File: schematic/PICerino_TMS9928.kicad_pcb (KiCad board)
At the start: 2 copper layers, 101.7 x 107.1 mm, 61 parts, among them CON1 PICERINO-EDGE, J1 Conn_01x02, J10 Conn_01x08, J11 Conn_01x08, J12 Conn_01x03, J2 Y_Conn_01x02, J3 BY_Conn_01x02, J4 RY_Conn_01x02, J7 Conn_01x02, J8 Conn_01x02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

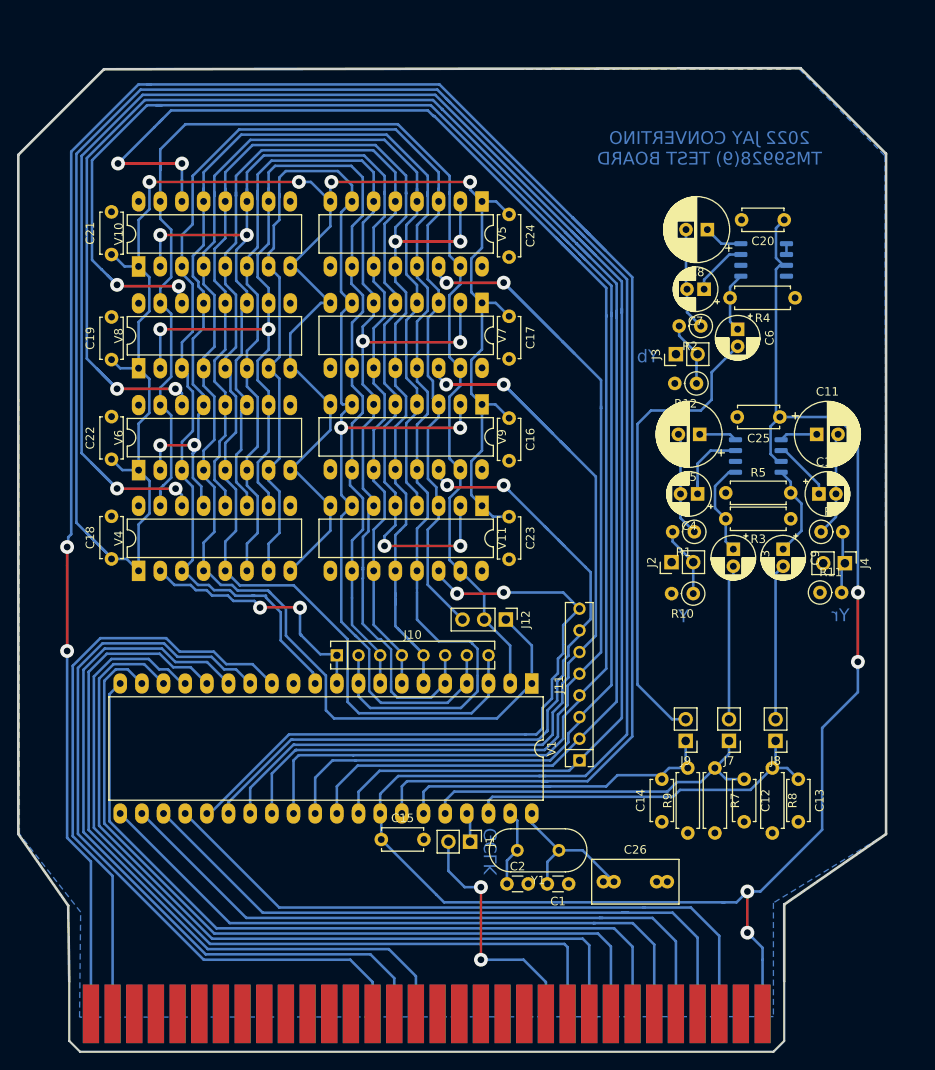
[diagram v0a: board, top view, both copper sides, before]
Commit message: updated schematic of TMS9928. This will work for 9918, and 9929 as well. Only Y is needed for 9918, and 9929 requires a different crystal. One item to point out is this video circuit is only supposed to be a buffer AC output. This isn't correct for Y on the component video. It does work with the retrotink-2x and gefen component to hdmi converters. haven't tested for a strong blue issue yet, doesn't seem to do that. Also jumpers are inserted on the board to bring out TMS99XX video signals out to whatever video circuit is desired
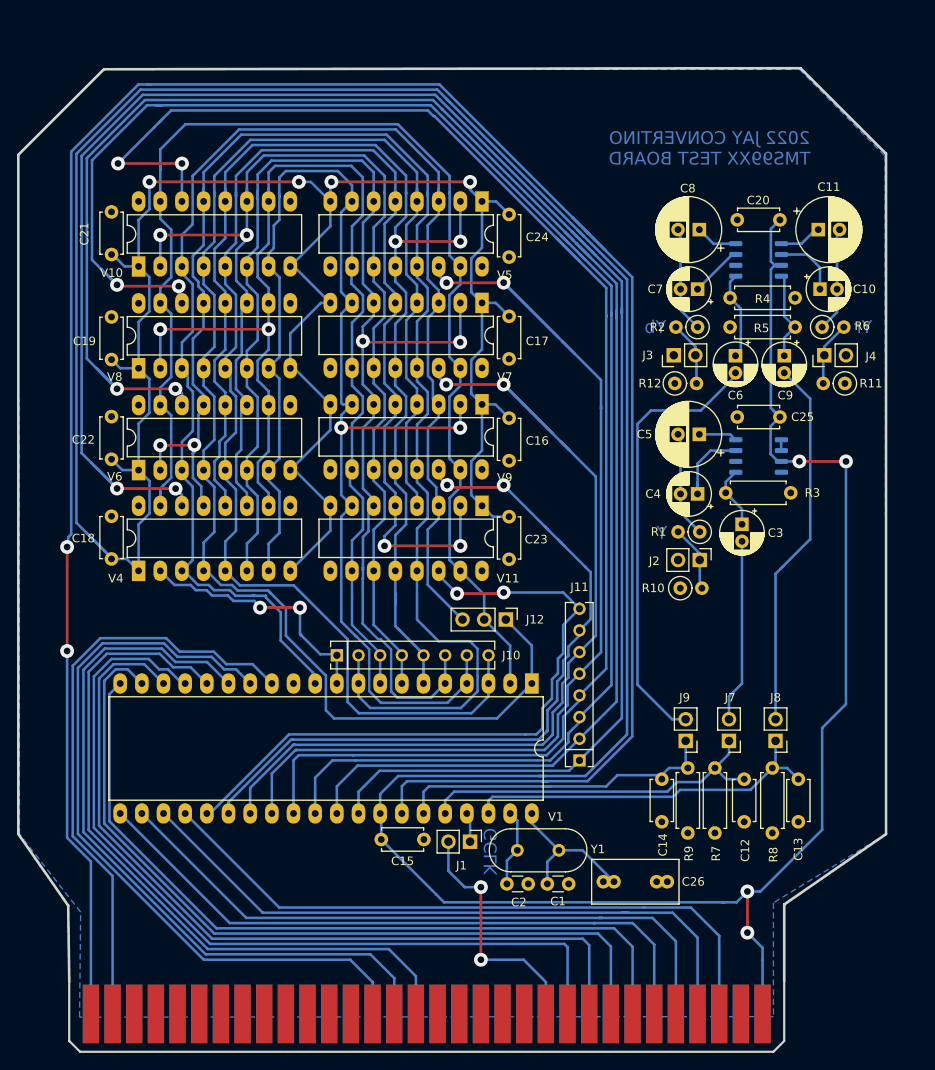
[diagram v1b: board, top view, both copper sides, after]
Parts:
- moved R11 24.7 mm to (202.9, 75.9), turned to 180 degrees
- moved J4 24.5 mm to (200.5, 72.6), turned to 90 degrees
- moved C11 24.0 mm to (199.8, 57.9)
- moved C10 24.0 mm to (200.0, 64.9)
- moved R6 24.0 mm to (200.3, 69.3)
- moved C9 22.7 mm to (195.8, 72.7)
- moved R5 19.4 mm to (189.5, 69.3)
- moved R4 7.62 mm to (189.5, 65.9), turned to 0 degrees
- moved J2 3.31 mm to (185.9, 96.6), turned to 270 degrees
- moved C6 3.12 mm to (190.1, 72.7)
- moved C3 3.09 mm to (190.9, 92.5)
- moved R3 3.05 mm to (196.6, 88.8)
- moved R12 2.54 mm to (183.0, 75.9), turned to 0 degrees
- moved R10 1.65 mm to (183.6, 99.9), turned to 0 degrees
- moved C8 0.94 mm to (185.9, 57.9)
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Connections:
- J2 pad 1: VSS -> Net-(J2-Pad1)
- J2 pad 2: Net-(J2-Pad2) -> VSS
- R1 pad 2: Net-(J2-Pad2) -> Net-(J2-Pad1)
- R10 pad 1: Net-(J2-Pad2) -> VSS
- R10 pad 2: Net-(R10-Pad2) -> Net-(J2-Pad1)
- R12 pad 1: Net-(J3-Pad2) -> VSS
- R12 pad 2: VSS -> Net-(J3-Pad2)
- R4 pad 1: VSS -> Net-(C6-Pad1)
- R4 pad 2: Net-(C6-Pad1) -> VSS
- V2 pad 5: Net-(C11-Pad1) -> Net-(V2-Pad5)
- V2 pad 6: Net-(C10-Pad1) -> Net-(V2-Pad5)
- V2 pad 8: Net-(C9-Pad1) -> VSS
- V3 pad 5: Net-(V3-Pad5) -> Net-(C11-Pad1)
- V3 pad 6: Net-(V3-Pad5) -> Net-(C10-Pad1)
- V3 pad 8: VSS -> Net-(C9-Pad1)
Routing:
- net Net-(C9-Pad2): track 18.3 -> 43.9 mm
- net Net-(J2-Pad2): track 8.60 -> 0.00 mm
- net Net-(J2-Pad1): track 0.00 -> 7.76 mm
- net VCC: track 608.0 -> 604.1 mm
- net Net-(C3-Pad2): track 18.1 -> 21.5 mm
- net Net-(C6-Pad1): track 7.11 -> 10.4 mm
- net Net-(C6-Pad2): track 55.3 -> 52.1 mm
- net Net-(C3-Pad1): track 11.4 -> 8.26 mm
- net Net-(V3-Pad5): track 1.27 -> 0.00 mm
- net Net-(V2-Pad5): track 0.00 -> 1.27 mm
- net Net-(C7-Pad2): track 12.0 -> 12.8 mm
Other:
- board text added: "2022 JAY CONVERTINO TMS99XX TEST BOARD"
- board text removed: "2022 JAY CONVERTINO TMS9928(9) TEST BOARD"

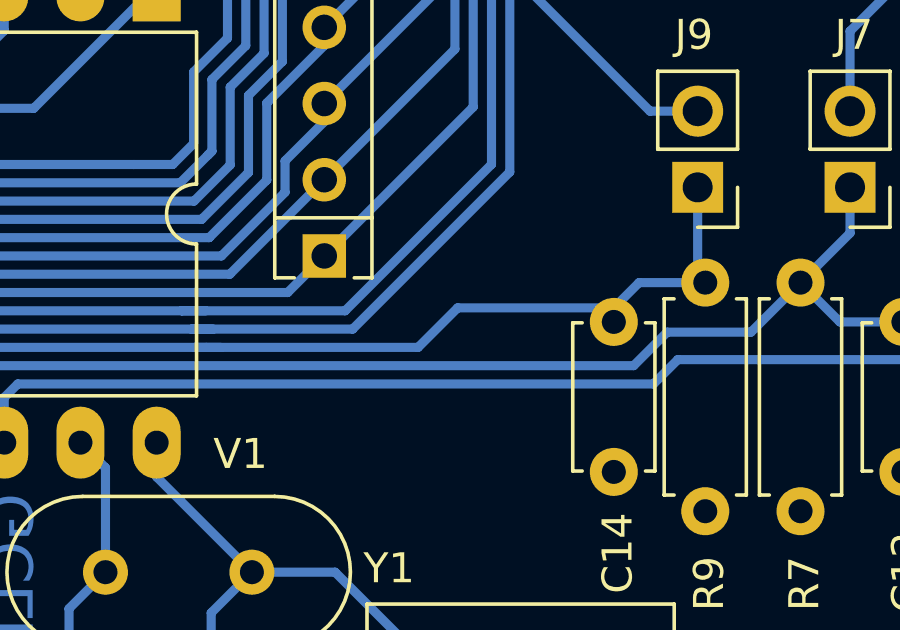
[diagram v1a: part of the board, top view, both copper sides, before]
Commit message: schematic cleanup in progress. changed address/write data lines to bus. cleaned up some component stuffs.
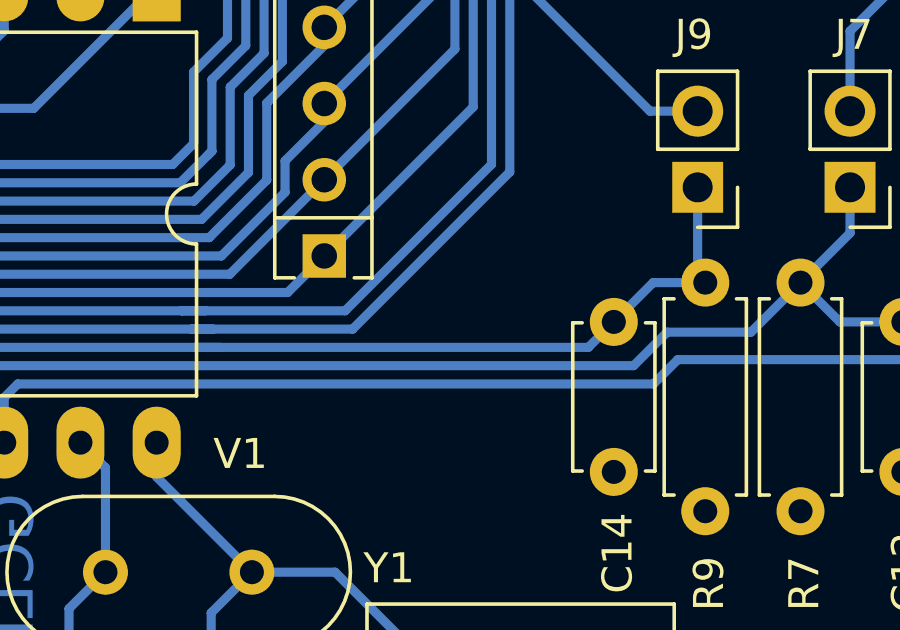
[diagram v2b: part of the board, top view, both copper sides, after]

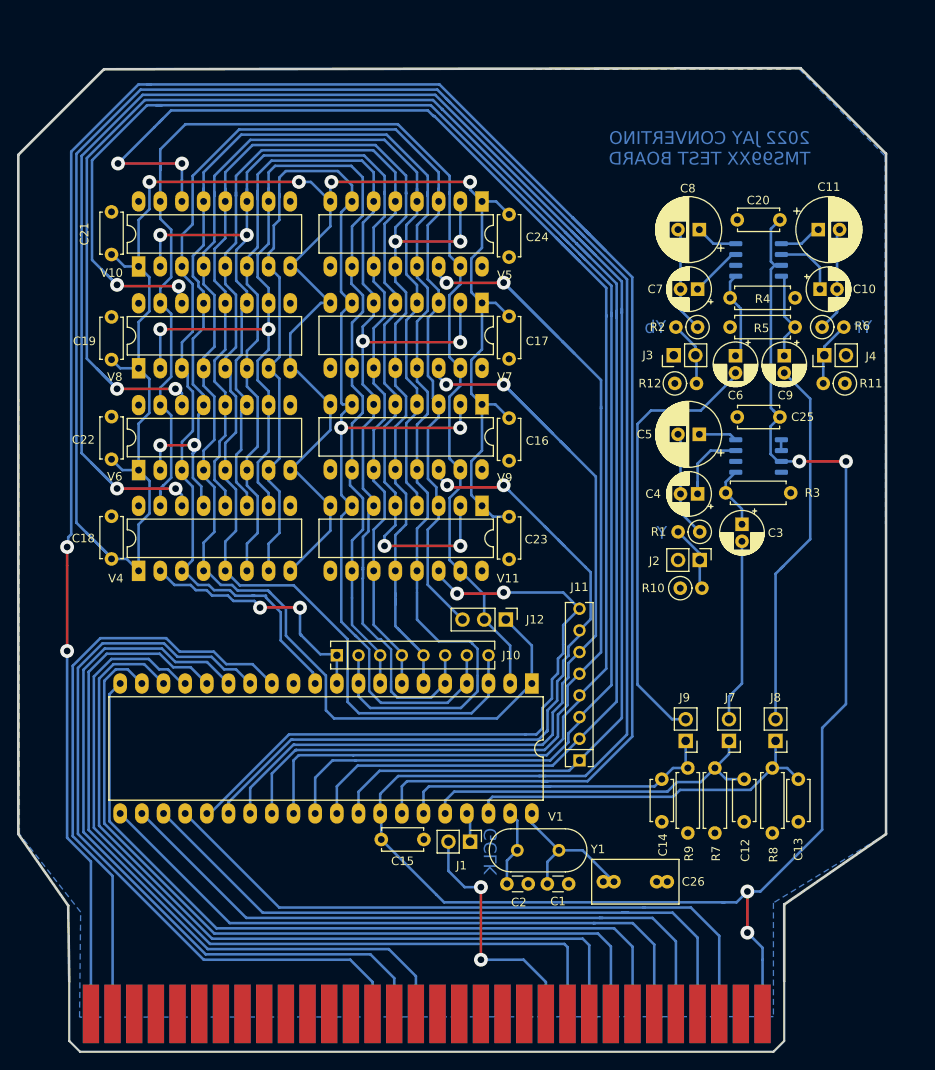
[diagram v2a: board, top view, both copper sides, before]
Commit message: major change to video section. dark green seemed off. tested adg453 sending output to gnd on that negative sync pulse. worked well. using mostly ti's idea with a modern sync strip ic. decided to use the other left over video opamp for a dc output. not tested at all but will be interesting since Y is supposed to be dc offset (works as ac offset though...whatever). This is intended to be a adjustable and usable for both the 9918 and 9928.
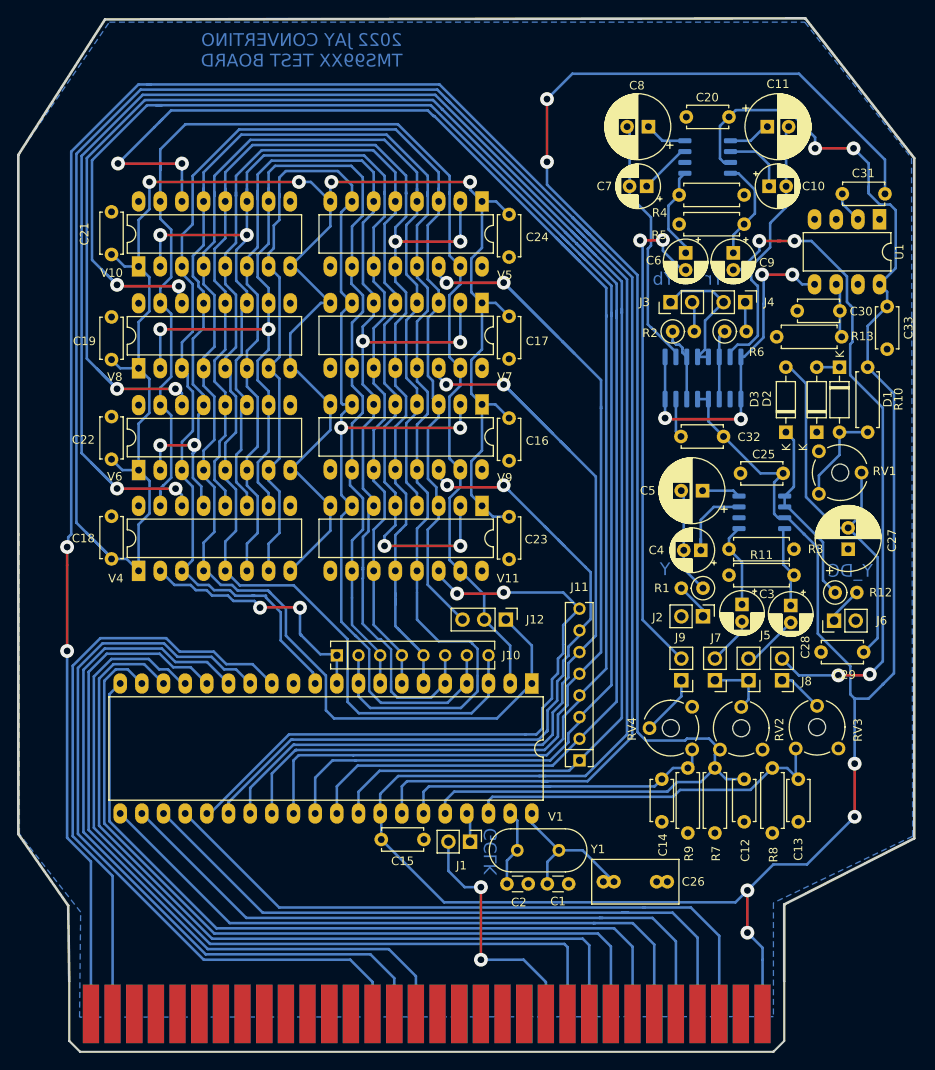
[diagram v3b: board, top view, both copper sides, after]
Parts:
- added C27: 100uF, Capacitor_THT:CP_Radial_D7.5mm_P2.50mm, F.Cu at (203.3, 95.4)
- added C28: 10uF, Capacitor_THT:CP_Radial_D5.0mm_P2.00mm, F.Cu at (196.6, 102.0)
- added C29: 100nF, Capacitor_THT:C_Disc_D4.7mm_W2.5mm_P5.00mm, F.Cu at (200.2, 107.4)
- added C30: 100nF, Capacitor_THT:C_Disc_D4.7mm_W2.5mm_P5.00mm, F.Cu at (197.4, 67.4)
- added C31: 100nF, Capacitor_THT:C_Disc_D4.7mm_W2.5mm_P5.00mm, F.Cu at (207.6, 53.7)
- added C32: 100nF, Capacitor_THT:C_Disc_D4.7mm_W2.5mm_P5.00mm, F.Cu at (188.7, 82.2)
- added C33: 100nF, Capacitor_THT:C_Disc_D4.7mm_W2.5mm_P5.00mm, F.Cu at (207.9, 66.9)
- added D1: 1N914, Diode_THT:D_DO-35_SOD27_P7.62mm_Horizontal, F.Cu at (202.3, 74.0)
- added D2: 1N914, Diode_THT:D_DO-35_SOD27_P7.62mm_Horizontal, F.Cu at (199.6, 81.7)
- added D3: 1N914, Diode_THT:D_DO-35_SOD27_P7.62mm_Horizontal, F.Cu at (196.0, 81.7)
- added IC1: ADG453BNZ, Package_SO:SOIC-16_3.9x9.9mm_P1.27mm, B.Cu at (186.3, 75.3)
- added J5: Conn_01x02, Connector_PinHeader_2.54mm:PinHeader_1x02_P2.54mm_Vertical, F.Cu at (191.6, 110.7)
- added J6: Y_Conn_DC_FIX_01x02, Connector_PinHeader_2.54mm:PinHeader_1x02_P2.54mm_Vertical, F.Cu at (201.7, 103.8)
- added R13: 680K, Resistor_THT:R_Axial_DIN0207_L6.3mm_D2.5mm_P7.62mm_Horizontal, F.Cu at (202.6, 70.5)
- added RV1: 100R, Potentiometer_THT:Potentiometer_Piher_PT-6-V_Vertical_Hole, F.Cu at (199.9, 88.9)
- added RV2: 10K, Potentiometer_THT:Potentiometer_Piher_PT-6-V_Vertical_Hole, F.Cu at (193.3, 118.9)
- added RV3: 10K, Potentiometer_THT:Potentiometer_Piher_PT-6-V_Vertical_Hole, F.Cu at (202.2, 118.7)
- added RV4: 10K, Potentiometer_THT:Potentiometer_Piher_PT-6-V_Vertical_Hole, F.Cu at (185.0, 113.9)
- added U1: LM1881, Package_DIP:DIP-8_W7.62mm_LongPads, F.Cu at (207.0, 56.7)
- C3: value 4.7uF -> 10uF
- R10: value 75R -> 470R; footprint Resistor_THT:R_Axial_DIN0207_L6.3mm_D2.5mm_P2.54mm_Vertical -> Resistor_THT:R_Axial_DIN0207_L6.3mm_D2.5mm_P7.62mm_Horizontal
- R11: value 75R -> 1M; footprint Resistor_THT:R_Axial_DIN0207_L6.3mm_D2.5mm_P2.54mm_Vertical -> Resistor_THT:R_Axial_DIN0207_L6.3mm_D2.5mm_P7.62mm_Horizontal
- moved R10 34.0 mm to (205.6, 74.0), turned to 270 degrees
- moved R12 30.9 mm to (201.8, 100.5)
- moved R11 26.3 mm to (189.4, 98.4), turned to 0 degrees
- moved R4 13.5 mm to (183.5, 53.8)
- moved R5 13.5 mm to (183.5, 57.3)
- moved C10 13.5 mm to (194.1, 52.8)
- moved C7 13.5 mm to (179.7, 52.8)
- moved V3 13.5 mm to (186.9, 49.4)
- moved C11 13.5 mm to (193.8, 45.8)
- moved C20 13.5 mm to (189.4, 44.7)
- moved C8 13.5 mm to (179.9, 45.8)
- moved C9 13.5 mm to (189.9, 60.6)
- moved C6 13.4 mm to (184.3, 60.6)
- moved R6 11.4 mm to (188.8, 69.8)
- moved J4 11.2 mm to (191.3, 66.4), turned to 270 degrees
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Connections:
- J7 pad 1: /Y -> Net-(J5-Pad1)
- J8 pad 1: /Yr -> Net-(J8-Pad1)
- J9 pad 1: /Yb -> Net-(J9-Pad1)
- R10 pad 1: VSS -> VCC
- R10 pad 2: Net-(J2-Pad1) -> Net-(D1-Pad2)
- R11 pad 2: Net-(J4-Pad1) -> Net-(C28-Pad1)
- R12 pad 1: VSS -> Net-(D3-Pad1)
- R12 pad 2: Net-(J3-Pad2) -> Net-(J6-Pad1)
- R2 pad 1: Net-(C7-Pad2) -> Net-(IC1-Pad14)
- R6 pad 1: Net-(C10-Pad2) -> Net-(IC1-Pad11)
- V2 pad 5: Net-(V2-Pad5) -> Net-(D3-Pad1)
- V2 pad 6: Net-(V2-Pad5) -> Net-(D3-Pad1)
- V2 pad 8: VSS -> Net-(C28-Pad1)
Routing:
- net /Y: track 42.6 -> 179.8 mm, vias 0 -> 2
- net VCC: track 604.1 -> 681.0 mm, vias 8 -> 10
- net Net-(C27-Pad2): track 0.00 -> 46.7 mm
- net Net-(IC1-Pad1): track 0.00 -> 41.1 mm, vias 0 -> 4
- net Net-(C9-Pad2): track 43.9 -> 78.2 mm, vias 0 -> 4
- net Net-(D3-Pad1): track 0.00 -> 22.3 mm
- net VSS: track 29.0 -> 50.2 mm
- net Net-(C10-Pad2): track 12.7 -> 31.3 mm
- net Net-(C7-Pad2): track 12.8 -> 29.7 mm
- net Net-(C3-Pad2): track 21.5 -> 5.67 mm
- net Net-(D1-Pad2): track 0.00 -> 11.5 mm
- net Net-(C28-Pad1): track 0.00 -> 9.76 mm
- net Net-(IC1-Pad14): track 0.00 -> 8.84 mm
- net Net-(IC1-Pad11): track 0.00 -> 8.20 mm
- net Net-(J5-Pad1): track 0.00 -> 7.42 mm
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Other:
- board size 101.7 x 107.1 mm -> 105 x 112.9 mm
- board text added: "Y_DC"
